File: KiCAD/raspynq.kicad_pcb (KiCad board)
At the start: 2 copper layers, 65 x 56 mm, 5 parts, among them P1 Conn_02x20_Odd_Even

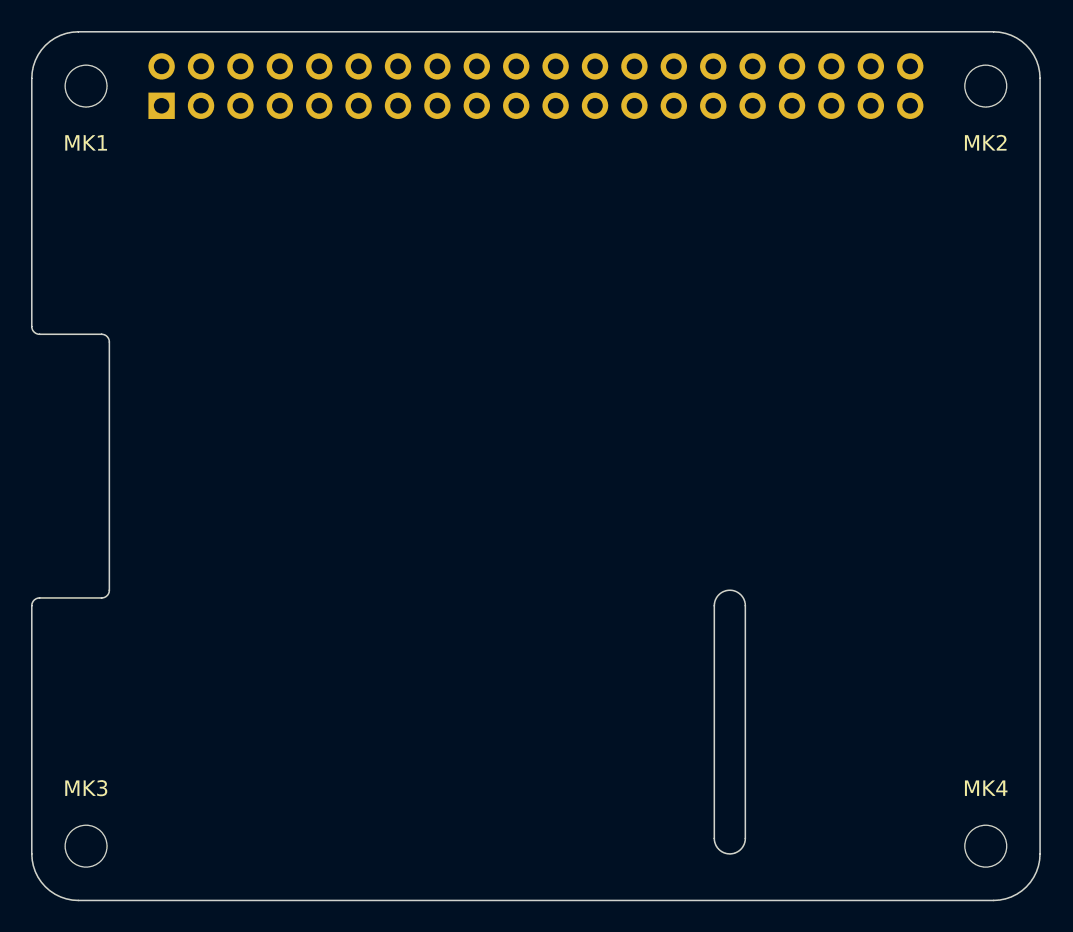
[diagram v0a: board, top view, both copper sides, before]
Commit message: gave up routing. decided to divide two boards (JTAG and others).
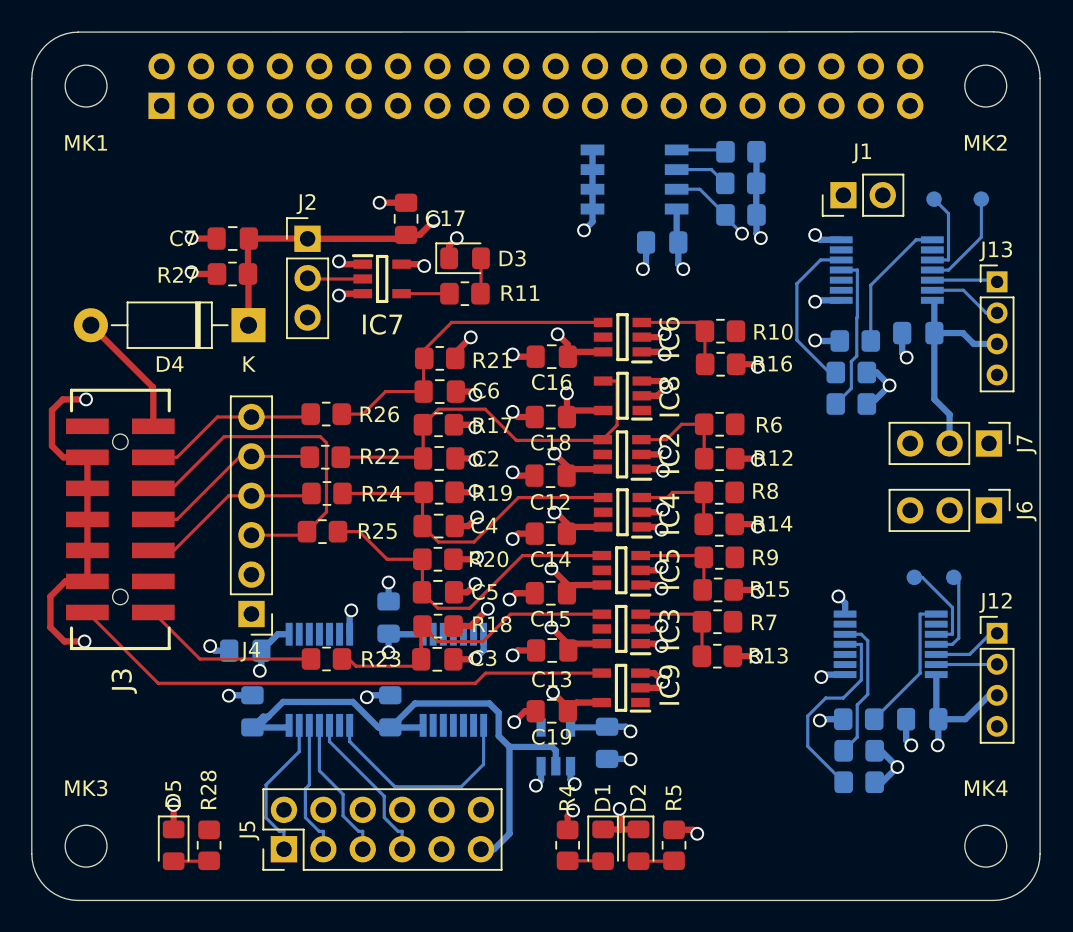
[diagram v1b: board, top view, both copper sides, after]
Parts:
- added C1: 0.1u, Capacitor_SMD:C_0805_2012Metric_Pad1.18x1.45mm_HandSolder, B.Cu at (240.6, 107.6)
- added C12: 0.1u, Capacitor_SMD:C_0805_2012Metric_Pad1.18x1.45mm_HandSolder, F.Cu at (233.4, 122.6)
- added C13: 0.1u, Capacitor_SMD:C_0805_2012Metric_Pad1.18x1.45mm_HandSolder, F.Cu at (233.5, 133.9)
- added C14: 0.1u, Capacitor_SMD:C_0805_2012Metric_Pad1.18x1.45mm_HandSolder, F.Cu at (233.5, 126.4)
- added C15: 0.1u, Capacitor_SMD:C_0805_2012Metric_Pad1.18x1.45mm_HandSolder, F.Cu at (233.5, 130.2)
- added C16: 0.1u, Capacitor_SMD:C_0805_2012Metric_Pad1.18x1.45mm_HandSolder, F.Cu at (233.5, 114.9)
- added C17: 0.1u, Capacitor_SMD:C_0805_2012Metric_Pad1.18x1.45mm_HandSolder, F.Cu at (224.1, 106.1)
- added C18: 0.1u, Capacitor_SMD:C_0805_2012Metric_Pad1.18x1.45mm_HandSolder, F.Cu at (233.5, 118.8)
- added C19: 0.1u, Capacitor_SMD:C_0805_2012Metric_Pad1.18x1.45mm_HandSolder, F.Cu at (233.5, 137.8)
- added C2: 100p, Capacitor_SMD:C_0805_2012Metric_Pad1.18x1.45mm_HandSolder, F.Cu at (226.3, 121.5)
- added C21: 0.1u, Capacitor_SMD:C_0805_2012Metric_Pad1.18x1.45mm_HandSolder, B.Cu at (237.1, 139.8)
- added C22: 0.1u, Capacitor_SMD:C_0805_2012Metric_Pad1.18x1.45mm_HandSolder, B.Cu at (223.1, 137.8)
- added C23: 0.1u, Capacitor_SMD:C_0805_2012Metric_Pad1.18x1.45mm_HandSolder, B.Cu at (214.2, 137.8)
- added C24: 0.1u, Capacitor_SMD:C_0805_2012Metric_Pad1.18x1.45mm_HandSolder, B.Cu at (257.4, 138.3)
- added C25: 0.1u, Capacitor_SMD:C_0805_2012Metric_Pad1.18x1.45mm_HandSolder, B.Cu at (257.1, 113.4)
- added C3: 100p, Capacitor_SMD:C_0805_2012Metric_Pad1.18x1.45mm_HandSolder, F.Cu at (226.1, 134.5)
- added C4: 100p, Capacitor_SMD:C_0805_2012Metric_Pad1.18x1.45mm_HandSolder, F.Cu at (226.2, 125.9)
- added C5: 100p, Capacitor_SMD:C_0805_2012Metric_Pad1.18x1.45mm_HandSolder, F.Cu at (226.2, 130.1)
- added C6: 100p, Capacitor_SMD:C_0805_2012Metric_Pad1.18x1.45mm_HandSolder, F.Cu at (226.3, 117.2)
- added C7: 100p, Capacitor_SMD:C_0805_2012Metric_Pad1.18x1.45mm_HandSolder, F.Cu at (213.0, 107.3)
- added C8: 0.1u, Capacitor_SMD:C_0805_2012Metric_Pad1.18x1.45mm_HandSolder, B.Cu at (223.0, 131.8)
- added C9: 0.1u, Capacitor_SMD:C_0805_2012Metric_Pad1.18x1.45mm_HandSolder, B.Cu at (213.8, 133.9)
- added D1: LED, LED_SMD:LED_0805_2012Metric_Pad1.15x1.40mm_HandSolder, F.Cu at (236.8, 146.4)
- added D2: LED, LED_SMD:LED_0805_2012Metric_Pad1.15x1.40mm_HandSolder, F.Cu at (239.1, 146.4)
- added D3: LED, LED_SMD:LED_0805_2012Metric_Pad1.15x1.40mm_HandSolder, F.Cu at (227.9, 108.6)
- added D4: 1N5817, Diode_THT:D_DO-41_SOD81_P10.16mm_Horizontal, F.Cu at (214.0, 112.9)
- added D5: LED, LED_SMD:LED_0805_2012Metric_Pad1.15x1.40mm_HandSolder, F.Cu at (209.1, 146.4)
- added IC1: CAT24C32WI-GT3, LibraryLoader:SOIC127P600X175-8N, B.Cu at (238.9, 103.5)
- added IC10: TXB0104PWRG4, LibraryLoader:SOP65P640X120-14N, B.Cu at (218.5, 135.8)
- added IC11: TXB0104PWRG4, LibraryLoader:SOP65P640X120-14N, B.Cu at (227.2, 135.8)
- added IC12: SN74LV1T125DBVR, LibraryLoader:SOT95P280X145-5N, B.Cu at (233.8, 140.1)
- added IC13: TXB0104PWRG4, LibraryLoader:SOP65P640X120-14N, B.Cu at (255.4, 133.5)
- added IC14: TXB0104PWRG4, LibraryLoader:SOP65P640X120-14N, B.Cu at (255.1, 109.4)
- added IC2: SN74LVC1T45DBVRE4, LibraryLoader:SOT95P280X145-6N, F.Cu at (238.1, 121.2)
- added IC3: SN74LVC1T45DBVRE4, LibraryLoader:SOT95P280X145-6N, F.Cu at (238.0, 132.5)
- added IC4: SN74LVC1T45DBVRE4, LibraryLoader:SOT95P280X145-6N, F.Cu at (238.1, 125.0)
- added IC5: SN74LVC1T45DBVRE4, LibraryLoader:SOT95P280X145-6N, F.Cu at (238.0, 128.7)
- added IC6: SN74LVC1T45DBVRE4, LibraryLoader:SOT95P280X145-6N, F.Cu at (238.1, 113.7)
- added IC7: SN74LV1T125DBVR, LibraryLoader:SOT95P280X145-5N, F.Cu at (222.6, 109.9)
- added IC8: SN74LV1T125DBVR, LibraryLoader:SOT95P280X145-5N, F.Cu at (238.1, 117.5)
- added IC9: SN74LV1T125DBVR, LibraryLoader:SOT95P280X145-5N, F.Cu at (238.0, 136.3)
- added J1: Conn_01x02, Connector_PinHeader_2.54mm:PinHeader_1x02_P2.54mm_Vertical, F.Cu at (252.3, 104.5)
- added J10: Conn_01x01, TestPoint:TestPoint_Pad_D1.0mm, B.Cu at (261.2, 104.8)
- added J11: Conn_01x01, TestPoint:TestPoint_Pad_D1.0mm, B.Cu at (258.2, 104.8)
- added J12: Conn_01x04, Connector_PinHeader_2.00mm:PinHeader_1x04_P2.00mm_Vertical, F.Cu at (262.2, 132.8)
- added J13: Conn_01x04, Connector_PinHeader_2.00mm:PinHeader_1x04_P2.00mm_Vertical, F.Cu at (262.2, 110.1)
- added J2: Conn_01x03, Connector_PinHeader_2.54mm:PinHeader_1x03_P2.54mm_Vertical, F.Cu at (217.8, 107.3)
- added J3: 87832-1420, LibraryLoader:87832-1420, F.Cu at (205.7, 125.4)
- added J4: Conn_01x06, Connector_PinHeader_2.54mm:PinHeader_1x06_P2.54mm_Vertical, F.Cu at (214.2, 131.5)
- added J5: Conn_02x06_Odd_Even, Connector_PinHeader_2.54mm:PinHeader_2x06_P2.54mm_Vertical, F.Cu at (216.3, 146.7)
- added J6: Conn_01x03, Connector_PinHeader_2.54mm:PinHeader_1x03_P2.54mm_Vertical, F.Cu at (261.7, 124.9)
- added J7: Conn_01x03, Connector_PinHeader_2.54mm:PinHeader_1x03_P2.54mm_Vertical, F.Cu at (261.7, 120.5)
- added J8: Conn_01x01, TestPoint:TestPoint_Pad_D1.0mm, B.Cu at (259.4, 129.2)
- added J9: Conn_01x01, TestPoint:TestPoint_Pad_D1.0mm, B.Cu at (256.9, 129.2)
- added R1: 3.9k, Resistor_SMD:R_0805_2012Metric_Pad1.20x1.40mm_HandSolder, B.Cu at (245.7, 101.7)
- added R10: 0, Resistor_SMD:R_0805_2012Metric_Pad1.20x1.40mm_HandSolder, F.Cu at (244.4, 113.3)
- added R11: 220, Resistor_SMD:R_0805_2012Metric_Pad1.20x1.40mm_HandSolder, F.Cu at (227.9, 110.9)
- added R12: 3.9k, Resistor_SMD:R_0805_2012Metric_Pad1.20x1.40mm_HandSolder, F.Cu at (244.3, 121.5)
- added R13: 3.9k, Resistor_SMD:R_0805_2012Metric_Pad1.20x1.40mm_HandSolder, F.Cu at (244.2, 134.3)
- added R14: 3.9k, Resistor_SMD:R_0805_2012Metric_Pad1.20x1.40mm_HandSolder, F.Cu at (244.3, 125.7)
- added R15: 3.9k, Resistor_SMD:R_0805_2012Metric_Pad1.20x1.40mm_HandSolder, F.Cu at (244.2, 130.0)
- added R16: 3.9k, Resistor_SMD:R_0805_2012Metric_Pad1.20x1.40mm_HandSolder, F.Cu at (244.4, 115.4)
- added R17: 5.9k, Resistor_SMD:R_0805_2012Metric_Pad1.20x1.40mm_HandSolder, F.Cu at (226.2, 119.3)
- added R18: 5.9k, Resistor_SMD:R_0805_2012Metric_Pad1.20x1.40mm_HandSolder, F.Cu at (226.2, 132.3)
- added R19: 5.9k, Resistor_SMD:R_0805_2012Metric_Pad1.20x1.40mm_HandSolder, F.Cu at (226.3, 123.7)
- added R2: 3.9k, Resistor_SMD:R_0805_2012Metric_Pad1.20x1.40mm_HandSolder, B.Cu at (245.7, 103.8)
- added R20: 5.9k, Resistor_SMD:R_0805_2012Metric_Pad1.20x1.40mm_HandSolder, F.Cu at (226.2, 128.0)
- added R21: 5.9k, Resistor_SMD:R_0805_2012Metric_Pad1.20x1.40mm_HandSolder, F.Cu at (226.3, 115.1)
- added R22: 100, Resistor_SMD:R_0805_2012Metric_Pad1.20x1.40mm_HandSolder, F.Cu at (218.9, 121.4)
- added R23: 100, Resistor_SMD:R_0805_2012Metric_Pad1.20x1.40mm_HandSolder, F.Cu at (219.0, 134.4)
- added R24: 100, Resistor_SMD:R_0805_2012Metric_Pad1.20x1.40mm_HandSolder, F.Cu at (219.0, 123.8)
- added R25: 100, Resistor_SMD:R_0805_2012Metric_Pad1.20x1.40mm_HandSolder, F.Cu at (218.7, 126.2)
- added R26: 100, Resistor_SMD:R_0805_2012Metric_Pad1.20x1.40mm_HandSolder, F.Cu at (219.0, 118.6)
- added R27: 1k, Resistor_SMD:R_0805_2012Metric_Pad1.20x1.40mm_HandSolder, F.Cu at (212.9, 109.6)
- added R28: 220, Resistor_SMD:R_0805_2012Metric_Pad1.20x1.40mm_HandSolder, F.Cu at (211.4, 146.4)
- added R29: 10k, Resistor_SMD:R_0805_2012Metric_Pad1.20x1.40mm_HandSolder, B.Cu at (253.3, 140.3)
- added R3: 1k, Resistor_SMD:R_0805_2012Metric_Pad1.20x1.40mm_HandSolder, B.Cu at (245.7, 105.8)
- added R30: 10k, Resistor_SMD:R_0805_2012Metric_Pad1.20x1.40mm_HandSolder, B.Cu at (252.8, 116.0)
- added R31: 10k, Resistor_SMD:R_0805_2012Metric_Pad1.20x1.40mm_HandSolder, B.Cu at (253.3, 142.4)
- added R32: 10k, Resistor_SMD:R_0805_2012Metric_Pad1.20x1.40mm_HandSolder, B.Cu at (252.8, 118.0)
- added R33: 10k, Resistor_SMD:R_0805_2012Metric_Pad1.20x1.40mm_HandSolder, B.Cu at (253.3, 138.3)
- added R34: 10k, Resistor_SMD:R_0805_2012Metric_Pad1.20x1.40mm_HandSolder, B.Cu at (253.1, 113.9)
- added R4: 220, Resistor_SMD:R_0805_2012Metric_Pad1.20x1.40mm_HandSolder, F.Cu at (234.5, 146.4)
- added R5: 220, Resistor_SMD:R_0805_2012Metric_Pad1.20x1.40mm_HandSolder, F.Cu at (241.4, 146.4)
- added R6: 0, Resistor_SMD:R_0805_2012Metric_Pad1.20x1.40mm_HandSolder, F.Cu at (244.3, 119.3)
- added R7: 0, Resistor_SMD:R_0805_2012Metric_Pad1.20x1.40mm_HandSolder, F.Cu at (244.2, 132.0)
- added R8: 0, Resistor_SMD:R_0805_2012Metric_Pad1.20x1.40mm_HandSolder, F.Cu at (244.3, 123.7)
- added R9: 0, Resistor_SMD:R_0805_2012Metric_Pad1.20x1.40mm_HandSolder, F.Cu at (244.3, 127.9)
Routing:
- net GND: track 0.00 -> 610.9 mm, vias 0 -> 43
- net +3V3: track 0.00 -> 273.6 mm, vias 0 -> 23
- net VCC: track 0.00 -> 166.4 mm, vias 0 -> 13
- net +5V: track 0.00 -> 160.4 mm, vias 0 -> 1
- net /raspynq_gpio/VIO: track 0.00 -> 37.8 mm
- net Net-(IC9-Pad4): track 0.00 -> 35.3 mm
- net Net-(C2-Pad2): track 0.00 -> 25.4 mm
- net /serial_interface/VI2C: track 0.00 -> 24.5 mm, vias 0 -> 1
- net Net-(J3-Pad6): track 0.00 -> 22.6 mm
- net Net-(C5-Pad2): track 0.00 -> 21.8 mm
- net Net-(C3-Pad2): track 0.00 -> 21.4 mm
- net Net-(C6-Pad2): track 0.00 -> 20.9 mm
- net Net-(C4-Pad2): track 0.00 -> 20.6 mm
- net /serial_interface/VUART: track 0.00 -> 14.0 mm
- net /GPIO26: track 0.00 -> 14.0 mm
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- added copper zone on In1.Cu, net +3V3
- added copper zone on In2.Cu, net GND
- added copper zone on In1.Cu, net VCC
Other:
- outline, holes or cut-outs redrawn
- copper layers 2 -> 4
- net class Default removed
- net class Power removed
